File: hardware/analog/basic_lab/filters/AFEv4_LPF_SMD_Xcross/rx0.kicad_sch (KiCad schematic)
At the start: 2 parts, among them J7 Connector_Generic_Conn_01x02, J8 Connector_Generic_Conn_01x02

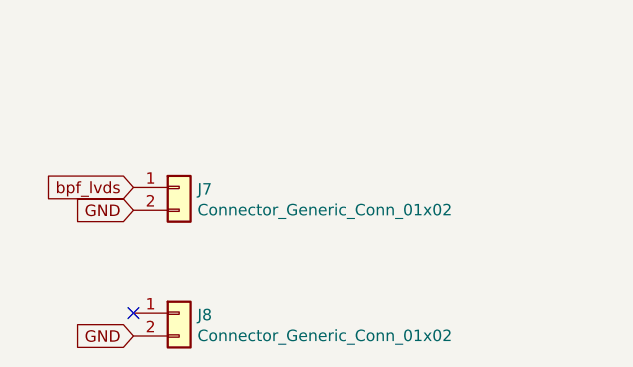
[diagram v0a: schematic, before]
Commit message: started PCB LPF LC SMD
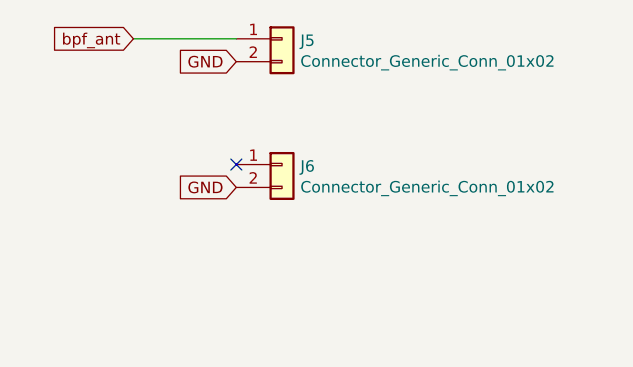
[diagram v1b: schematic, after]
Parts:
- removed J7, J8: Connector_Generic_Conn_01x02, Connector_PinHeader_2.54mm:PinHeader_1x02_P2.54mm_Vertical, symbol bgt:Connector_Generic_Conn_01x02
- added J5, J6: Connector_Generic_Conn_01x02, Connector_PinHeader_2.54mm:PinHeader_1x02_P2.54mm_Vertical, symbol bgt:Connector_Generic_Conn_01x02
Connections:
- net GND: now also J5.2 (Pin_2), J6.2 (Pin_2)
- new net bpf_ant: J5.1 (Pin_1)
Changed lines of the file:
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@@
 (kicad_sch (version 20211123) (generator eeschema)
   (paper "A4")
-  (no_connect (at 162.56 114.3))
-  (global_label "GND" (shape input) (at 162.56 116.84 180) (fields_autoplaced)
+  (no_connect (at 173.99 97.79))
+  (wire (pts (xy 162.56 83.82) (xy 173.99 83.82))
+    (stroke (width 0) (type default) (color 0 0 0 0))
+  )
+  (global_label "GND" (shape input) (at 173.99 100.33 180) (fields_autoplaced)
     (effects (font (size 1.27 1.27)) (justify right))
-    (property "Intersheet References" "${INTERSHEET_REFS}" (id 0) (at 1.27 -17.78 0)
+    (property "Intersheet References" "${INTERSHEET_REFS}" (id 0) (at 12.7 -34.29 0)
       (effects (font (size 1.27 1.27)) hide)
     )
   )
-  (global_label "GND" (shape input) (at 162.56 102.87 180) (fields_autoplaced)
+  (global_label "GND" (shape input) (at 173.99 86.36 180) (fields_autoplaced)
     (effects (font (size 1.27 1.27)) (justify right))
-    (property "Intersheet References" "${INTERSHEET_REFS}" (id 0) (at 1.27 -31.75 0)
+    (property "Intersheet References" "${INTERSHEET_REFS}" (id 0) (at 12.7 -48.26 0)
       (effects (font (size 1.27 1.27)) hide)
     )
   )
-  (global_label "bpf_lvds" (shape input) (at 162.56 100.33 180) (fields_autoplaced)
+  (global_label "bpf_ant" (shape input) (at 162.56 83.82 180) (fields_autoplaced)
     (effects (font (size 1.27 1.27)) (justify right))
-    (property "Intersheet References" "${INTERSHEET_REFS}" (id 0) (at 12.7 -31.75 0)
+    (property "Intersheet References" "${INTERSHEET_REFS}" (id 0) (at 379.73 163.83 0)
       (effects (font (size 1.27 1.27)) hide)
     )
   )
-  (symbol (lib_id "bgt:Connector_Generic_Conn_01x02") (at 167.64 114.3 0) (unit 1)
+  (symbol (lib_id "bgt:Connector_Generic_Conn_01x02") (at 179.07 83.82 0) (unit 1)
     (in_bom yes) (on_board yes)
-    (property "Reference" "J8" (id 0) (at 169.672 114.5032 0)
+    (property "Reference" "J5" (id 0) (at 181.102 84.0232 0)
       (effects (font (size 1.27 1.27)) (justify left))
     )
-    (property "Value" "Connector_Generic_Conn_01x02" (id 1) (at 169.672 116.8146 0)
+    (property "Value" "Connector_Generic_Conn_01x02" (id 1) (at 181.102 86.3346 0)
       (effects (font (size 1.27 1.27)) (justify left))
     )
-    (property "Footprint" "Connector_PinHeader_2.54mm:PinHeader_1x02_P2.54mm_Vertical" (id 2) (at 167.64 114.3 0)
+    (property "Footprint" "Connector_PinHeader_2.54mm:PinHeader_1x02_P2.54mm_Vertical" (id 2) (at 179.07 83.82 0)
       (effects (font (size 1.27 1.27)) hide)
     )
-    (property "Datasheet" "" (id 3) (at 167.64 114.3 0)
+    (property "Datasheet" "" (id 3) (at 179.07 83.82 0)
       (effects (font (size 1.27 1.27)) hide)
     )
@@
     (pin "2")
   )
-  (symbol (lib_id "bgt:Connector_Generic_Conn_01x02") (at 167.64 100.33 0) (unit 1)
+  (symbol (lib_id "bgt:Connector_Generic_Conn_01x02") (at 179.07 97.79 0) (unit 1)
     (in_bom yes) (on_board yes)
-    (property "Reference" "J7" (id 0) (at 169.672 100.5332 0)
+    (property "Reference" "J6" (id 0) (at 181.102 97.9932 0)
       (effects (font (size 1.27 1.27)) (justify left))
     )
-    (property "Value" "Connector_Generic_Conn_01x02" (id 1) (at 169.672 102.8446 0)
+    (property "Value" "Connector_Generic_Conn_01x02" (id 1) (at 181.102 100.3046 0)
       (effects (font (size 1.27 1.27)) (justify left))
     )
-    (property "Footprint" "Connector_PinHeader_2.54mm:PinHeader_1x02_P2.54mm_Vertical" (id 2) (at 167.64 100.33 0)
+    (property "Footprint" "Connector_PinHeader_2.54mm:PinHeader_1x02_P2.54mm_Vertical" (id 2) (at 179.07 97.79 0)
       (effects (font (size 1.27 1.27)) hide)
     )
-    (property "Datasheet" "" (id 3) (at 167.64 100.33 0)
+    (property "Datasheet" "" (id 3) (at 179.07 97.79 0)
       (effects (font (size 1.27 1.27)) hide)
     )
